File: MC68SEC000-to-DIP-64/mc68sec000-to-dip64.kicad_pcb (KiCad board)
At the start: 2 copper layers, 25.6 x 81.9 mm, 5 parts, among them U2 68010D

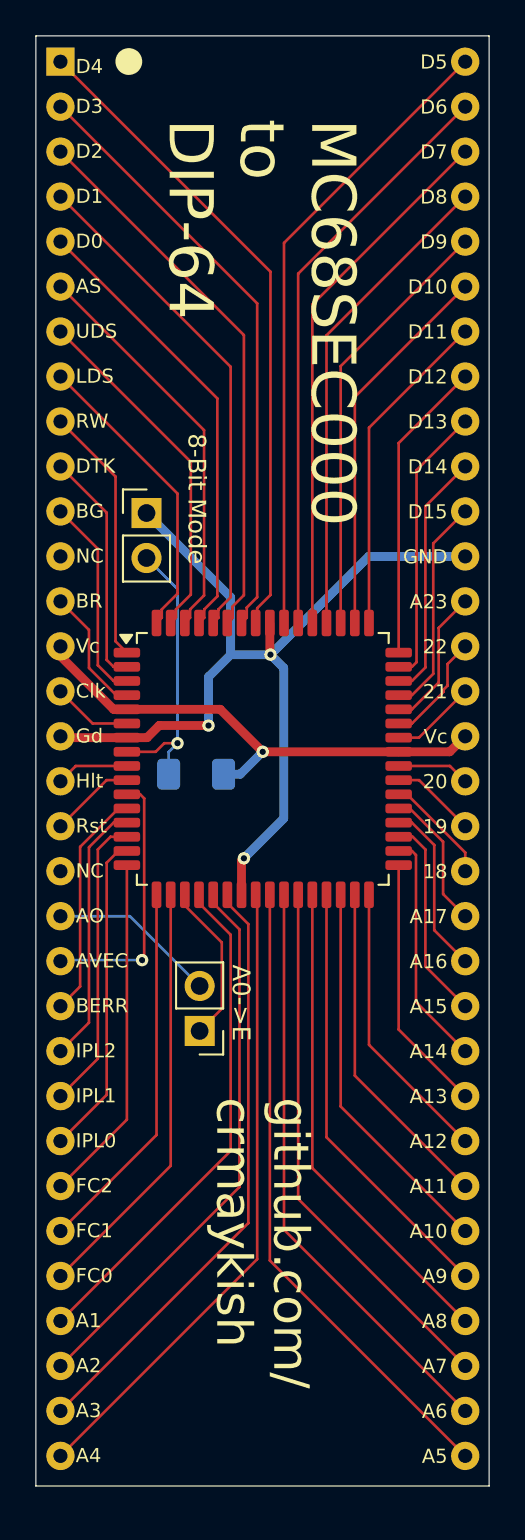
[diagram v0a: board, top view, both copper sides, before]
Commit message: Use larger footprint for MC68SEC000 QFP-64 IC
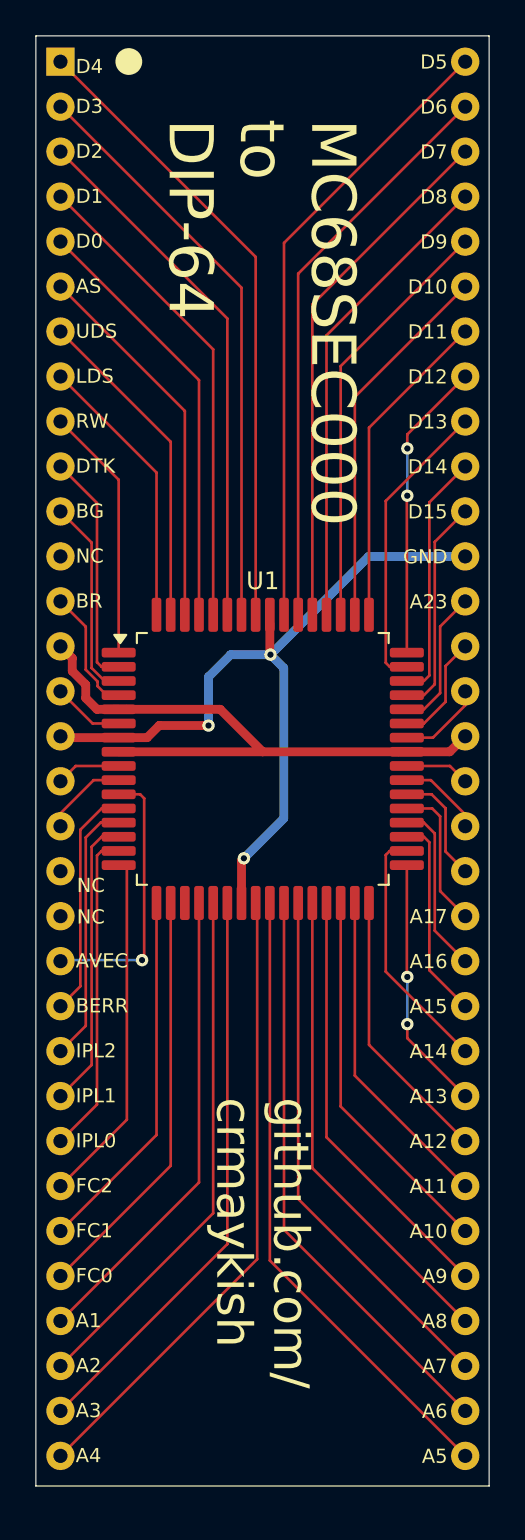
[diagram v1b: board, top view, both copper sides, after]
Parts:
- removed JP1, JP2: Jumper_2_Open, Connector_PinHeader_2.54mm:PinHeader_1x02_P2.54mm_Vertical
- removed R1: R, Resistor_SMD:R_1206_3216Metric_Pad1.30x1.75mm_HandSolder
- U1: footprint Package_QFP:LQFP-64_14x14mm_P0.8mm -> Package_QFP:PQFP-64_14x14mm_P0.8mm
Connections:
- U1 pad 8: Net-(JP1-B) -> VCC
- U2 pad 20: Net-(JP2-B) -> unconnected-(U2-E-Pad20)
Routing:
- net Net-(JP1-B): track 16.2 -> 0.00 mm, vias 1 -> 0
- net GND: track 55.4 -> 45.4 mm
- net Net-(JP2-B): track 9.49 -> 0.00 mm
- net /A0: track 9.07 -> 0.00 mm
- net VCC: track 28.7 -> 35.0 mm, vias 1 -> 0
- net /A1: track 28.8 -> 26.8 mm
- net /A2: track 31.4 -> 29.7 mm
- net //LDS: track 17.1 -> 15.7 mm
- net /A3: track 34.0 -> 32.6 mm
- net //UDS: track 20.0 -> 18.6 mm
- net //AS: track 22.8 -> 21.4 mm
- net /D0: track 25.6 -> 24.3 mm
- net /D1: track 28.5 -> 27.2 mm
- net /D2: track 31.3 -> 30.1 mm
- net /D3: track 34.1 -> 32.9 mm
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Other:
- board text removed: "18"
- board text removed: "19"
- board text removed: "20"
- board text removed: "21"
- board text removed: "22"
- board text removed: "8-Bit Mode"
- board text removed: "A0->E"
- board text removed: "AO"
- board text removed: "Clk"
- board text removed: "Gd"
- board text removed: "Hlt"
- board text removed: "Rst"
- board text removed: "Vc"
